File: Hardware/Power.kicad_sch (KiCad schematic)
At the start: 9 parts, among them IC2 LM74502HDDFR, Q1 PSMN8R5-40MSDX

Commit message: Firmware vA1
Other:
- note added: "Bah"
- note removed: "Bypass Cap"
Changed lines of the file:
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@@
 		)
 	)
-	(text "Bypass Cap"
+	(text " Bah\n"
 		(exclude_from_sim no)
 		(at 117.094 58.674 0)
@@
 		)
 		(property "Value" "LM74502HDDFR"
-			(at 67.31 60.325 0)
-			(effects
-				(font
+			(at 85.09 58.42 0)
+			(effects
+				(font

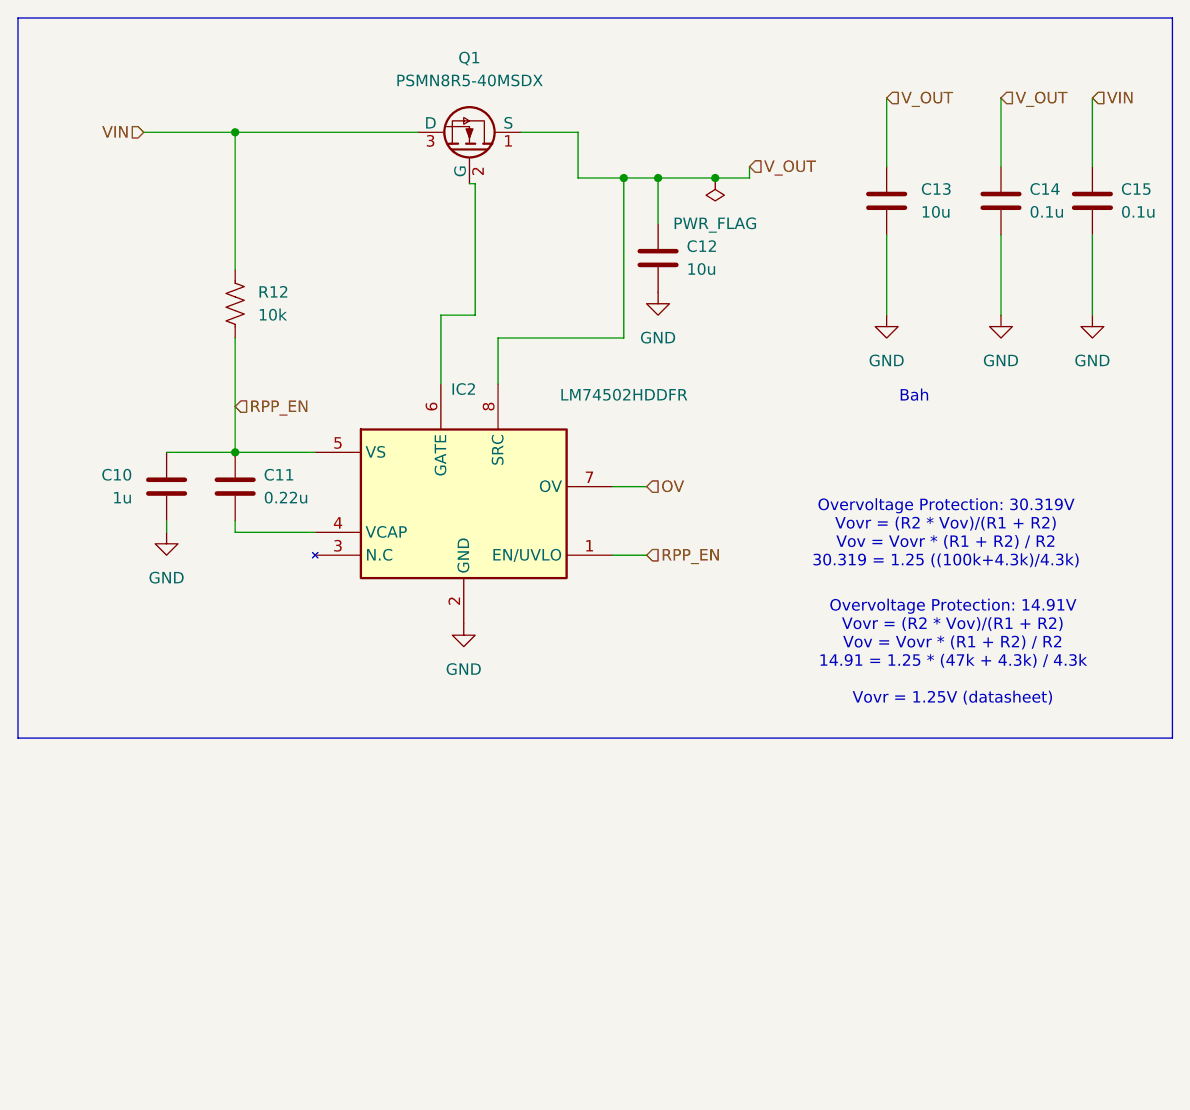
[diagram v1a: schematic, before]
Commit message: Bring Hardware folder from RevB
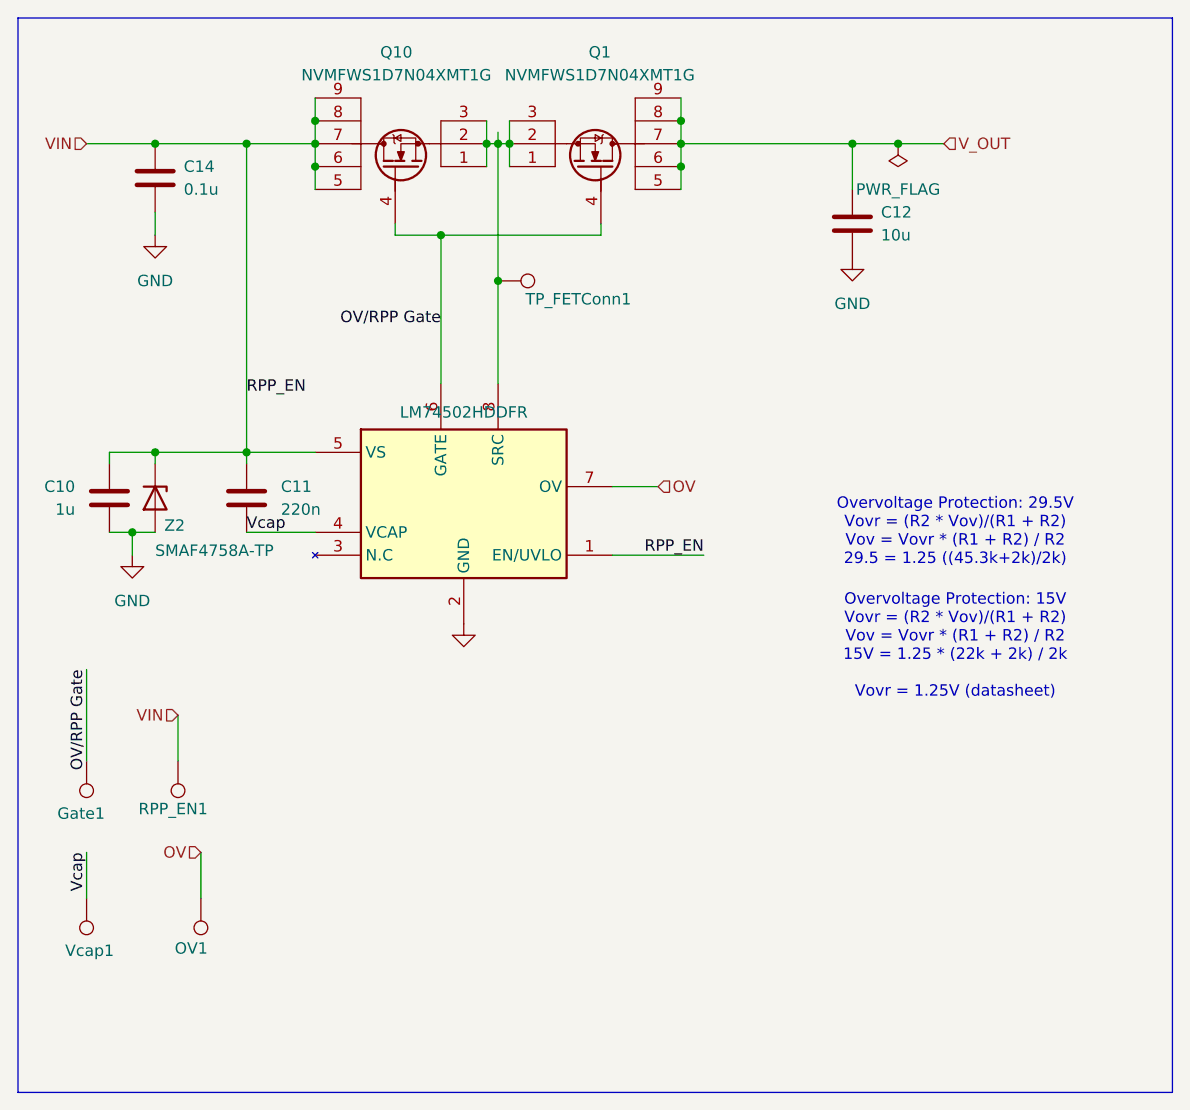
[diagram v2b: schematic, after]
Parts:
- removed C13: 10u, Capacitor_SMD:C_0805_2012Metric, symbol Device:C
- removed C15: 0.1u, Capacitor_SMD:C_0603_1608Metric, symbol Device:C
- removed Q1: PSMN8R5-40MSDX, UTSVT_Power:PSMN8R5-40MSDX, symbol utsvt_power:PSMN8R5-40MSDX
- removed R12: 10k, Resistor_SMD:R_0603_1608Metric, symbol Device:R_US
- added Gate1: TP_Gate, TestPoint:TestPoint_THTPad_D1.5mm_Drill0.7mm, symbol Connector:TestPoint
- added OV1, TP_FETConn1, Vcap1: TestPoint, TestPoint:TestPoint_THTPad_D1.5mm_Drill0.7mm, symbol Connector:TestPoint
- added Q1, Q10: NVMFWS1D7N04XMT1G, UTSVT_Power:NVMFWS3D0P04M8LT1G, symbol utsvt_misc:NVMFWS1D7N04XMT1G
- added RPP_EN1: TestPoint, TestPoint:TestPoint_THTPad_D3.0mm_Drill1.5mm, symbol Connector:TestPoint
- added Z2: SMAF4758A-TP, UTSVT_Passives:SODFL5026X125N, symbol Device:D_Zener
- C11: value 0.22u -> 220n
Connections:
- net RPP_EN is gone; now on net VIN: C10.2, C11.1, IC2.1 (EN/UVLO), IC2.5 (VS)
- net GND: now also Z2.2 (A)
- net OV: now also OV1.1
- net VIN: now also C14.1, Q10.5, Q10.6, Q10.7, Q10.8, Q10.9, RPP_EN1.1, Z2.1 (K)
- net V_OUT: now also Q1.5, Q1.6, Q1.7, Q1.8, Q1.9; no longer C14.1, IC2.8 (SRC)
- net Vcap: now reaches C11.2, IC2.4 (VCAP)
- net Vcap: now also Vcap1.1
- net OV/RPP Gate: now reaches IC2.6 (GATE)
- net OV/RPP Gate: now also Gate1.1, Q1.4, Q10.4
- new net: IC2.8 (SRC), Q1.1, Q1.2, Q1.3, Q10.1, Q10.2, Q10.3, TP_FETConn1.1
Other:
- note added: "Overvoltage Protection: 15V Vovr = (R2 * Vov)/(R1 + R2) Vov = Vovr * (R1 + R2) / R2 15V = 1.25 * (22k + 2k) / 2k Vovr = 1.25V (datasheet)"
- note added: "Overvoltage Protection: 29.5V Vovr = (R2 * Vov)/(R1 + R2) Vov = Vovr * (R1 + R2) / R2 29.5 = 1.25 ((45.3k+2k)/2k)"
- note removed: "Bah"
- note removed: "Overvoltage Protection: 14.91V Vovr = (R2 * Vov)/(R1 + R2) Vov = Vovr * (R1 + R2) / R2 14.91 = 1.25 * (47k + 4.3k) / 4.3k Vovr = 1.25V (datasheet)"
- note removed: "Overvoltage Protection: 30.319V Vovr = (R2 * Vov)/(R1 + R2) Vov = Vovr * (R1 + R2) / R2 30.319 = 1.25 ((100k+4.3k)/4.3k)"
- moved on the sheet: C10, C11, C12
